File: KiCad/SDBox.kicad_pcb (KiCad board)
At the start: 2 copper layers, 47 x 50 mm, 22 parts, among them J1 DB25_Male, J2 Micro_SD_Card_Socket, U1 ESP32-DEVKIT-V1, U2 SN74CB3T16210

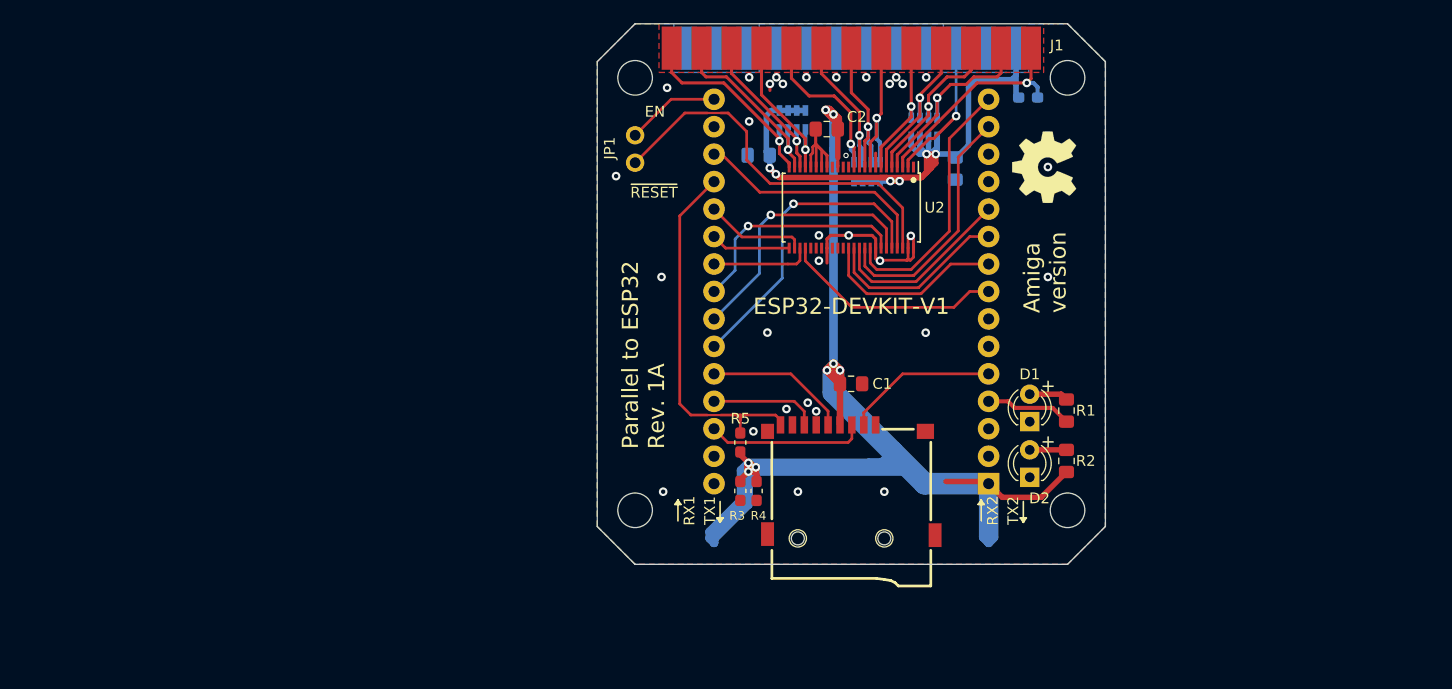
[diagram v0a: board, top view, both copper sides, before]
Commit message: Update design to accomodate a Rapberry_Pi_Pico_2W
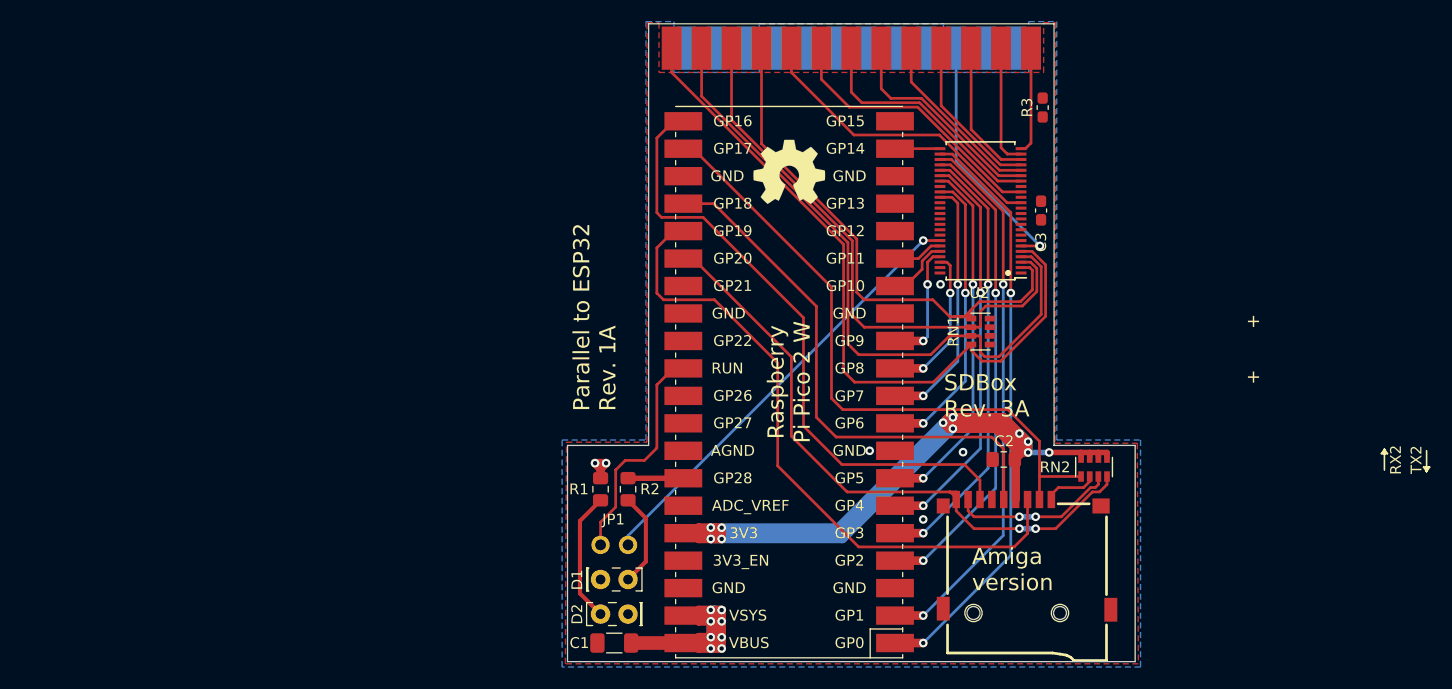
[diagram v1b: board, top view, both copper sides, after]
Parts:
- removed the C3 at (157.3, 98.4)
- removed C4: 0.1uF, Capacitor_SMD:C_0805_2012Metric_Pad1.15x1.40mm_HandSolder
- removed the R1 at (167.6, 120.8)
- removed the R3 at (137.4, 128.2)
- removed R4: 1k, Resistor_SMD:R_0603_1608Metric_Pad1.05x0.95mm_HandSolder
- removed R5: 10k, Resistor_SMD:R_0603_1608Metric_Pad1.05x0.95mm_HandSolder
- removed the RN1 at (154.4, 94.6)
- added C1: 10uF, Capacitor_SMD:C_1206_3216Metric_Pad1.33x1.80mm_HandSolder, F.Cu at (125.8, 142.3)
- added R2: 220, Resistor_SMD:R_0805_2012Metric_Pad1.15x1.40mm_HandSolder, F.Cu at (127.0, 128.1)
- C3: renamed from C2; footprint Capacitor_SMD:C_0805_2012Metric_Pad1.15x1.40mm_HandSolder -> Capacitor_SMD:C_0603_1608Metric_Pad1.08x0.95mm_HandSolder
- D1, D2: footprint LED_THT:LED_D3.0mm -> LED_THT:LED_Rectangular_W5.0mm_H2.0mm
- R1: renamed from R2; value 150 -> 220
- R3: renamed from R8; moved to F.Cu
- RN1: renamed from RN3; value 4.7k_R_Pack04 -> 10k_R_Pack04; footprint Parallel_to_ESP32:RESCAF80P320X160X60-8N -> SDBox:RESCAF80P320X160X60-8N; moved to F.Cu
- RN2: value 4.7k_R_Pack04 -> 10k_R_Pack04; footprint Parallel_to_ESP32:RESCAF80P320X160X60-8N -> SDBox:RESCAF80P320X160X60-8N; moved to F.Cu
- U1: value ESP32-DEVKIT-V1 -> Rapberry_Pi_Pico_2W; footprint SDBox:MODULE_ESP32_DEVKIT_V1 -> SDBox:RPi_Pico_SMD
- moved R1 43.2 mm to (124.5, 128.1), turned to 270 degrees
- moved D1 42.3 mm to (124.5, 136.4), turned to 0 degrees
- moved D2 39.2 mm to (127.0, 139.6), turned to 180 degrees
- moved JP1 38.0 mm to (124.5, 133.2), turned to 90 degrees
- moved RN2 34.5 mm to (170.2, 126.0), turned to 270 degrees
- moved RN1 26.2 mm to (159.7, 113.5), turned to 180 degrees
- moved REF** 23.6 mm to (141.9, 98.7), turned to 0 degrees
- moved C3 21.2 mm to (165.2, 102.3), turned to 270 degrees
- moved J2 17.7 mm to (163.9, 128.2)
- moved C2 15.8 mm to (161.8, 125.3), turned to 180 degrees
- moved U2 12.0 mm to (159.7, 102.3), turned to 180 degrees
- moved U1 8.40 mm to (141.9, 118.1)
- moved R3 1.64 mm to (165.4, 92.7), turned to 90 degrees
- renumbered C1 to C2
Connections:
- net RX1 renamed Net-(U1-Pad17)
- J1 pad 14: Amiga_5V -> Net-(J1-Pad14)
- J2 pad 1: Net-(J2-Pad1) -> NC1
- J2 pad 8: Net-(J2-Pad8) -> NC2
- JP1 pad 1: EN -> /RUN
- R1 pad 1: 3V3 -> VCC
- R3 pad 1: Amiga_5V -> VCC
- RN1 pad 1: Amiga_5V -> VCC
- RN1 pad 2: Amiga_5V -> VCC
- RN1 pad 3: Amiga_5V -> VCC
- RN1 pad 4: Amiga_5V -> VCC
- RN2 pad 1: Amiga_5V -> 3V3
- RN2 pad 2: Amiga_5V -> 3V3
- RN2 pad 3: Amiga_5V -> 3V3
- RN2 pad 4: Amiga_5V -> 3V3
- RN2 pad 5: D7 -> CS
- RN2 pad 6: D6 -> NC1
- RN2 pad 7: D5 -> NC2
- RN2 pad 8: D4 -> CP
- U1 pad 1: 3V3 -> D0_3V3
- U1 pad 10: D6_3V3 -> D7_3V3
- U1 pad 11: D5_3V3 -> ACK_3V3
- U1 pad 12: Net-(U1-Pad12) -> BUSY_3V3
- U1 pad 13: Net-(U1-Pad13) -> GND
- U1 pad 14: D4_3V3 -> POUT_3V3
- U1 pad 15: D3_3V3 -> SELECT_3V3
- U1 pad 16: EN -> Net-(U1-Pad16)
- U1 pad 18: STROBE_3V3 -> GND
- U1 pad 19: CP -> STROBE_3V3
- U1 pad 2: GND -> D1_3V3
- U1 pad 20: POUT_3V3 -> Net-(U1-Pad20)
- U1 pad 21: SELECT_3V3 -> MISO
- U1 pad 22: BUSY_3V3 -> CS
- U1 pad 23: D2_3V3 -> GND
- U1 pad 24: D1_3V3 -> SCK
- U1 pad 25: D0_3V3 -> MOSI
- U1 pad 26: SCK -> CP
- U1 pad 27: MISO -> Net-(U1-Pad27)
- U1 pad 28: MOSI -> GND
- U1 pad 29: GND -> Net-(U1-Pad29)
- U1 pad 3: TX1 -> GND
- U1 pad 30: Net-(U1-Pad30) -> /RUN
- U1 pad 4: ACT_LED -> D2_3V3
- U1 pad 5: CS -> D3_3V3
- U1 pad 6: RX2 -> D4_3V3
- U1 pad 7: TX2 -> D5_3V3
- U1 pad 8: ACK_3V3 -> GND
- U1 pad 9: D7_3V3 -> D6_3V3
- U2 pad 10: D5 -> Net-(U2-Pad10)
- U2 pad 11: D6 -> Net-(U2-Pad11)
- U2 pad 12: D7 -> Net-(U2-Pad12)
- U2 pad 14: GND -> D7
- U2 pad 16: GND -> D6
- U2 pad 18: GND -> D5
- U2 pad 19: GND -> D4
- U2 pad 2: RESET -> ACK
- U2 pad 20: GND -> D3
- U2 pad 21: ACK -> D2
- U2 pad 22: BUSY -> D1
- U2 pad 23: POUT -> D0
- U2 pad 24: SELECT -> STROBE
- U2 pad 25: SELECT_3V3 -> STROBE_3V3
- U2 pad 26: POUT_3V3 -> D0_3V3
- U2 pad 27: BUSY_3V3 -> D1_3V3
- U2 pad 28: ACK_3V3 -> D2_3V3
- U2 pad 29: Net-(U2-Pad29) -> D3_3V3
- U2 pad 3: STROBE -> BUSY
- U2 pad 30: Net-(U2-Pad30) -> D4_3V3
- U2 pad 31: Net-(U2-Pad31) -> D5_3V3
- U2 pad 33: Net-(U2-Pad33) -> D6_3V3
- U2 pad 34: Net-(U2-Pad34) -> D7_3V3
- U2 pad 36: D7_3V3 -> Net-(U2-Pad36)
- U2 pad 37: D6_3V3 -> Net-(U2-Pad37)
- U2 pad 38: D5_3V3 -> Net-(U2-Pad38)
- U2 pad 39: D4_3V3 -> Net-(U2-Pad39)
- U2 pad 4: D0 -> POUT
- U2 pad 40: D3_3V3 -> Net-(U2-Pad40)
- U2 pad 42: D2_3V3 -> RESET_3V3
- U2 pad 43: D1_3V3 -> SELECT_3V3
- U2 pad 44: D0_3V3 -> POUT_3V3
- U2 pad 45: STROBE_3V3 -> BUSY_3V3
- U2 pad 46: RESET_3V3 -> ACK_3V3
- U2 pad 5: D1 -> SELECT
- U2 pad 6: D2 -> RESET
- U2 pad 7: D3 -> Net-(U2-Pad7)
- U2 pad 9: D4 -> Net-(U2-Pad9)
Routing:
- net Amiga_5V: track 69.6 -> 0.00 mm, vias 6 -> 0
- net VCC: track 0.00 -> 49.1 mm, vias 0 -> 10
- net MISO: track 9.99 -> 58.7 mm
- net SELECT: track 18.8 -> 67.2 mm, vias 1 -> 0
- net MOSI: track 14.7 -> 61.4 mm
- net POUT: track 17.6 -> 61.9 mm, vias 1 -> 0
- net CS: track 14.7 -> 58.5 mm
- net 3V3: track 178.2 -> 139.3 mm, vias 8 -> 11
- net BUSY: track 14.7 -> 52.8 mm, vias 1 -> 0
- net ACK: track 14.6 -> 50.4 mm, vias 1 -> 0
- net SCK: track 13.8 -> 48.8 mm
- net GND: track 29.6 -> 0.00 mm, vias 32 -> 4
- net D0_3V3: track 28.5 -> 55.5 mm, vias 1 -> 2
- net D1_3V3: track 24.8 -> 51.8 mm, vias 1 -> 2
- net D2_3V3: track 21.2 -> 45.6 mm, vias 1 -> 2
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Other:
- board size 47 x 50 mm -> 52.5 x 59 mm
- rule pad_to_mask_clearance: 0.051 -> 0
- rule via_min_drill: 0.3 -> 0.4
- rule via_min_size: 0.4 -> 0.8
- board text added: "Raspberry Pi Pico 2 W"
- board text added: "SDBox Rev. 3A"
- board text removed: "3V3"
- board text removed: "EN"
- board text removed: "ESP32-DEVKIT-V1"
- board text removed: "GND"
- board text removed: "RX1"
- board text removed: "TX1"
- board text removed: "~RESET"

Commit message: Place and route R3
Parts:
- moved R3 0.41 mm to (165.2, 93.1)
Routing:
- net STROBE: track 9.91 -> 12.9 mm
- net 3V3: track 139.3 -> 141.7 mm
- net SELECT: track 67.2 -> 68.7 mm
- net CS: track 58.5 -> 59.8 mm
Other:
- board text added: "-"

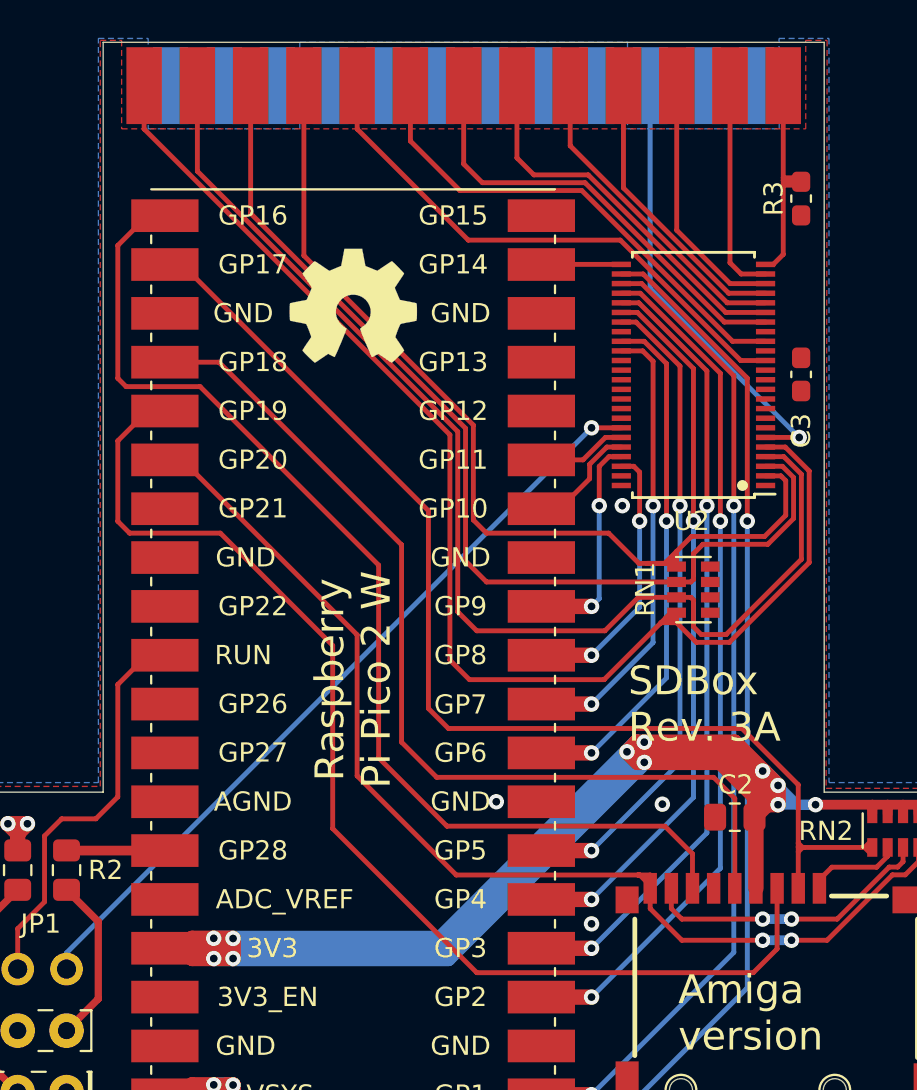
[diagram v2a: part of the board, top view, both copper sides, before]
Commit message: Add RN3 (pull-ups for data lines), fixed keep-out areas for header and test-points on RPi Pico 2 W
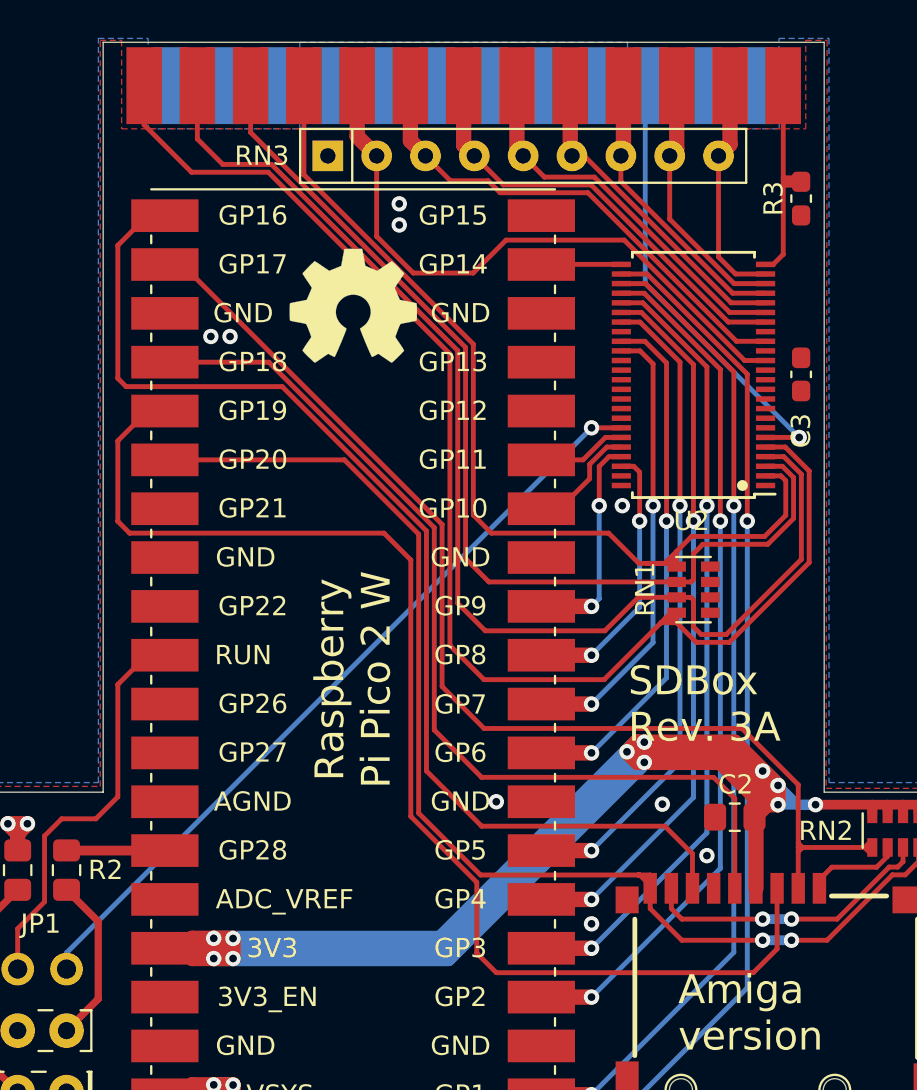
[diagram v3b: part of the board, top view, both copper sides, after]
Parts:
- added RN3: 10k, Resistor_THT:R_Array_SIP9, F.Cu at (140.6, 90.9)
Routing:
- net MOSI: track 61.4 -> 65.8 mm
- net CP: track 57.4 -> 61.6 mm
- net D7: track 28.5 -> 32.6 mm
- net SELECT: track 68.7 -> 70.6 mm
- net MISO: track 58.7 -> 60.1 mm
- net POUT: track 61.9 -> 63.1 mm
- net CS: track 59.8 -> 58.8 mm
- net D0: track 11.3 -> 12.0 mm
- net D5: track 23.2 -> 22.6 mm
- net GND: vias 4 -> 7
- net (no net): vias 0 -> 2
